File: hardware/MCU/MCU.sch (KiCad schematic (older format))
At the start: 45 parts, among them P1 CONN_01X05, P2 CONN_01X04, P3 CONN_01X05, P4 CONN_01X05, U1 MAX6369, U2 TC1262-30VDB, U3 DS18B20, U4 PIC18F45K22, U5 LT6005, Y1 Crystal

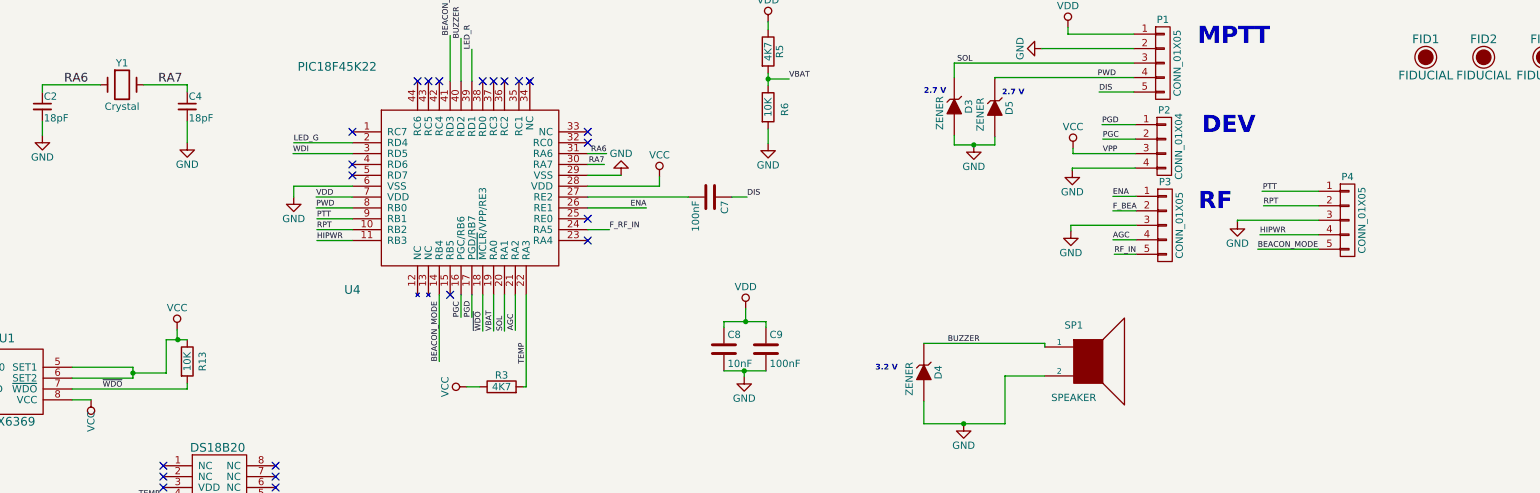
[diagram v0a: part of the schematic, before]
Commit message: Corregidos errores en el esquematico de la MCU: - Se incorpora el pin MCLR al conector de programacion (P2) y se ordenan acorde al pinout del programador PicKit 3 - La alimentación del microcontrolador del pin 7 se lleva a VCC.
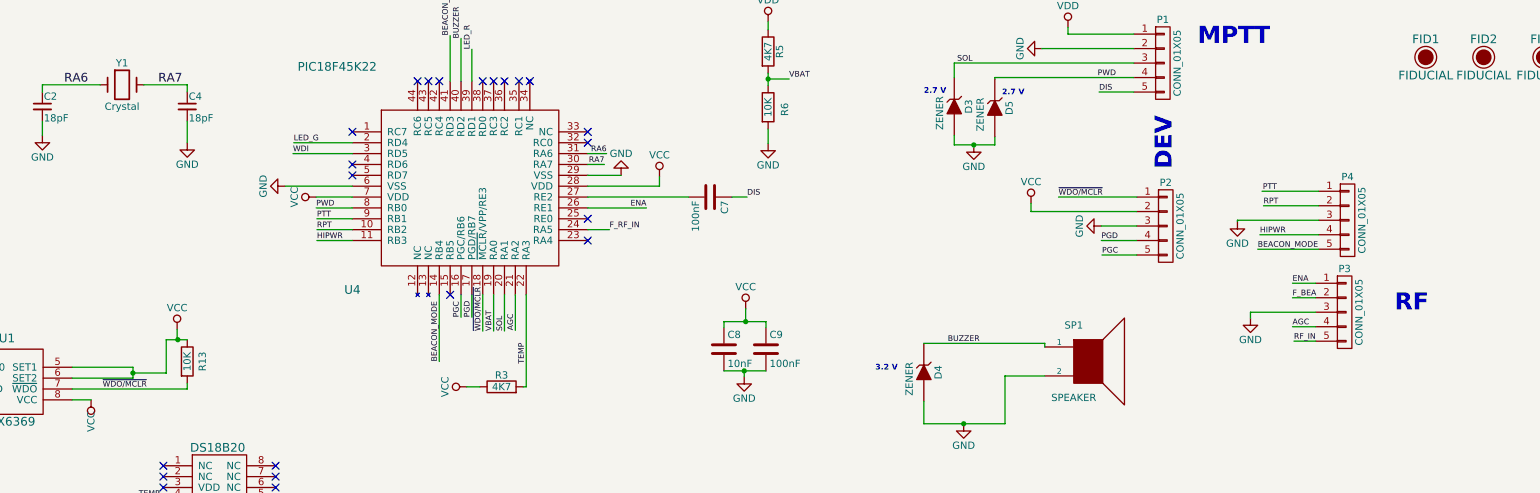
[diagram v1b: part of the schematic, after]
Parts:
- removed P2: CONN_01X04, Sockets_MOLEX_KK-System:Socket_MOLEX-KK-RM2-54mm_Lock_4pin_straight, symbol CONN_01X04
- added P2: CONN_01X05, Connectors_Terminal_Blocks:TerminalBlock_Pheonix_MPT-2.54mm_5pol, symbol CONN_01X05
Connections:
- net GND: now also P2.3 (P3)
- net PGC: now also P2.5 (P5)
- net PGD: now also P2.4 (P4)
- net VCC: now also C8.1, C9.1, U4.7 (VDD), P2.2 (P2)
- net VDD: no longer C8.1, C9.1, U4.7 (VDD)
- net ~WDO renamed ~WDO/MCLR
- net ~WDO/MCLR: now also P2.1 (P1)
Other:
- moved on the sheet: P3

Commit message: Reorganized schematics: different sections separated and clarified.
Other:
- note added: "Interfaces"
- note added: "LEDs"
- note added: "Mechanics"
- note added: "Power"
- note added: "Protections"
- moved on the sheet: C3, C5, D1, D2, D3, D4, D5, FID1, FID2, FID3, P1, P2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

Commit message: Added 3D models of header connectors
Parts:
- removed Y1: Crystal, Crystals:Crystal_HC49-4H_Vertical, symbol Crystal
- added X?: CRYSTAL_SMD, symbol CRYSTAL_SMD
- P1, P2, P3, P4: footprint Connectors_Terminal_Blocks:TerminalBlock_Pheonix_MPT-2.54mm_5pol -> Connectors_Molex:Molex_MicroLatch-53253-0570_05x2.00mm_Straight
- U2: footprint SOT-223 -> TO_SOT_Packages_SMD:SOT-223
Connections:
- net TEMP: now also R3.1; no longer R3.2
- net VCC: now also R3.2; no longer R3.1
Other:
- note added: "Buzzer"
- note added: "MCU"
- note added: "Temperature"
- note added: "Unused"
- note added: "Watchdog"
- moved on the sheet: C1, C10, C11, C12, C13, C2, C3, C4, C5, C6, C7, C8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

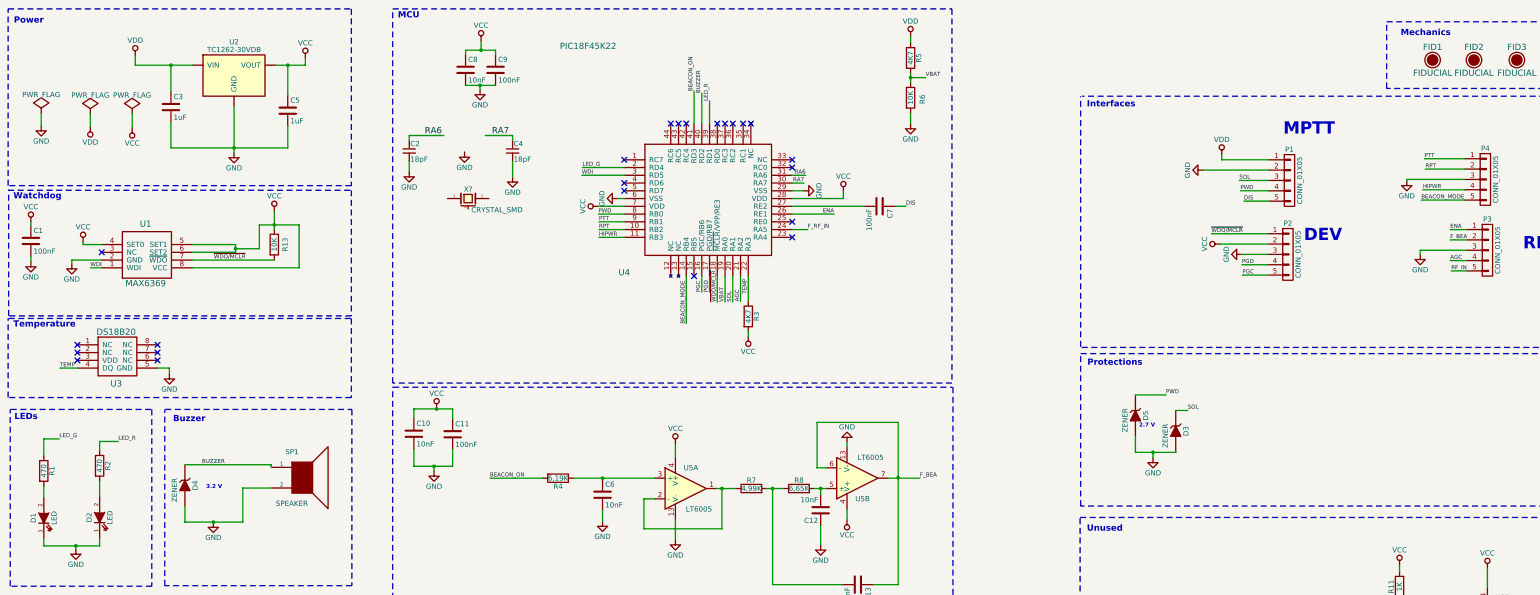
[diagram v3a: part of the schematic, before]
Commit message: Placement terminado para la versión 2.0 de la MCU
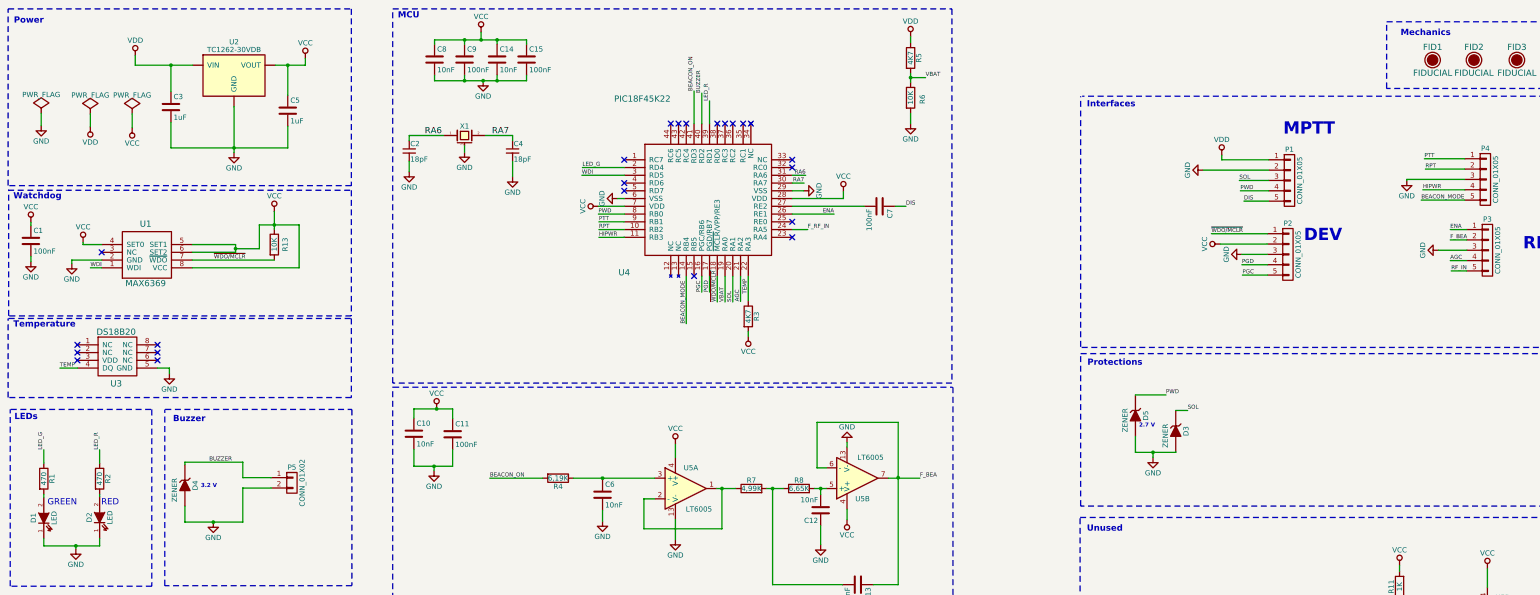
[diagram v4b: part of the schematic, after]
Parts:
- removed SP1: SPEAKER, Buzzers_Beepers:MagneticBuzzer_Kingstate_KCG0601, symbol SPEAKER
- added C14: 10nF, Capacitors_SMD:C_0603_HandSoldering, symbol C
- added C15: 100nF, Capacitors_SMD:C_0603_HandSoldering, symbol C
- added P5: CONN_01X02, Connectors_Molex:Molex_KK-6410-02_02x2.54mm_Straight, symbol CONN_01X02
- X1: renamed from X?; footprint (none) -> Crystals:Crystal_SMD_0603-4pin_6.0x3.5mm
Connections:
- net BUZZER: now also P5.1 (P1)
- net GND: now also X1.3 (case), C14.2, C15.2, P5.2 (P2)
- net RA6: now also X1.1
- net RA7: now also X1.2
- net VCC: now also C14.1, C15.1
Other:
- note added: "GREEN"
- note added: "RED"
- moved on the sheet: C8, C9, R1, R2, X1
